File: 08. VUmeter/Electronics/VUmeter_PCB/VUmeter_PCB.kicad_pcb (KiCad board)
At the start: 2 copper layers, 33 x 43.2 mm, 6 parts, among them J1 ESP32S3 SuperMini I, J2 ESP32S3 SuperMini D, J3 INMP4144 I, J4 INMP4144 D, J5 Tira LED, J6 Alimentacion

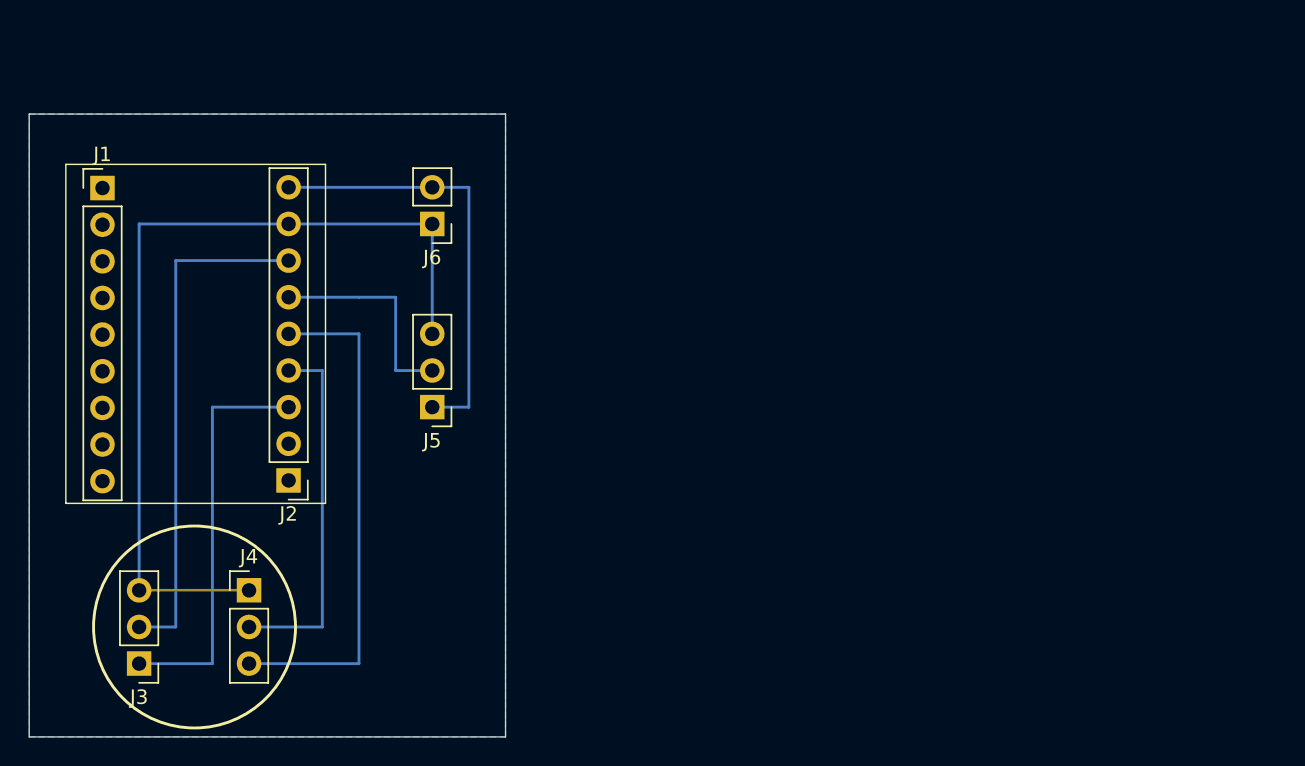
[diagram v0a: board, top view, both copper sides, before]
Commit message: 08.VUmeter. PCB update and Software update according to schematic.
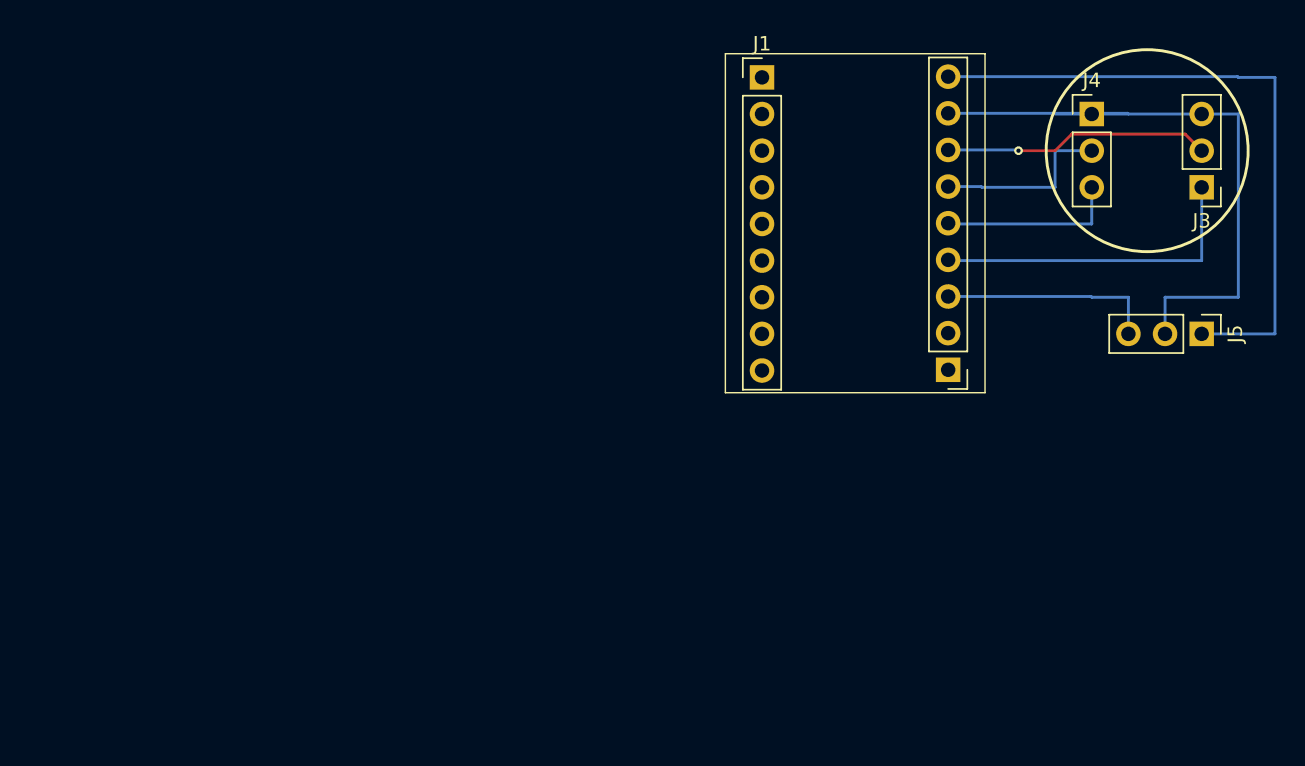
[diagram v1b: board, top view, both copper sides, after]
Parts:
- removed J6: Alimentacion, Connector_PinHeader_2.54mm:PinHeader_1x02_P2.54mm_Vertical
- moved J3 80.7 mm to (180.3, 68.6)
- moved J4 67.1 mm to (172.7, 63.5)
- moved J5 53.6 mm to (180.3, 78.7), turned to -90 degrees
- moved J1 46.4 mm to (149.9, 61.0)
- moved J2 46.4 mm to (162.8, 81.2)
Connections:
- J3 pad 1: /10 -> /11
- J4 pad 2: /11 -> /13
- J5 pad 2: /13 -> /GND
- J5 pad 3: /GND -> /10
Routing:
- net /12: track 35.4 -> 12.5 mm
- net /3V3: track 35.8 -> 18.6 mm, vias 0 -> 1
- net /GND: track 61.0 -> 45.5 mm
- net /5V: track 30.3 -> 45.5 mm
- net /10: track 28.1 -> 15.1 mm
- net /13: track 15.0 -> 12.5 mm
- net /11: track 25.2 -> 22.7 mm
- removed copper zone on B.Cu, net (none)
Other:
- board outline removed
